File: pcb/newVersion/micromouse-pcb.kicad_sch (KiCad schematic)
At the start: 40 parts, among them J1_MotorEncoder1 Conn_01x06, J2_MotorEncoder1 Conn_01x06, J3 Conn_01x08, J4 Conn_01x08, Q1 BS170, Q2 TEFT4300, Q3 BS170, Q4 TEFT4300, Q5 BS170, Q6 TEFT4300, Q7 BS170, Q8 TEFT4300, SW1 SW_SPDT, U0 Teensy 4.1, U2 L7805

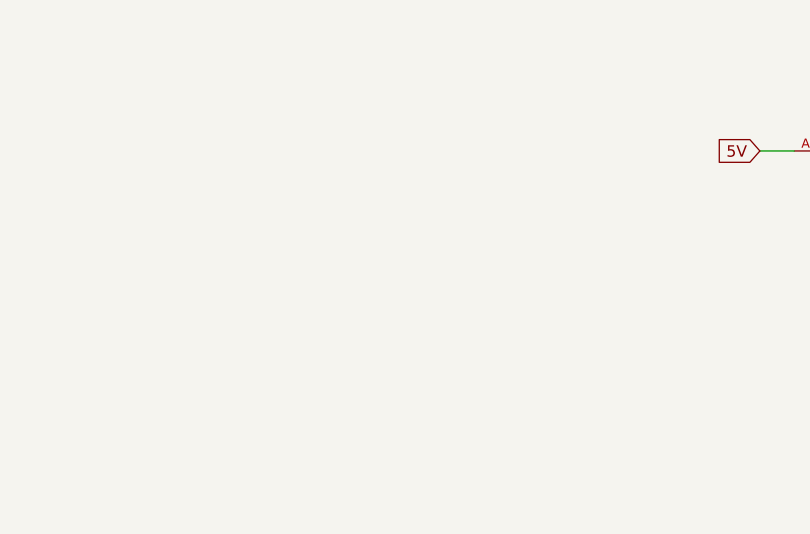
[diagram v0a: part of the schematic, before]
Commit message: changed board outline for ball caster mount
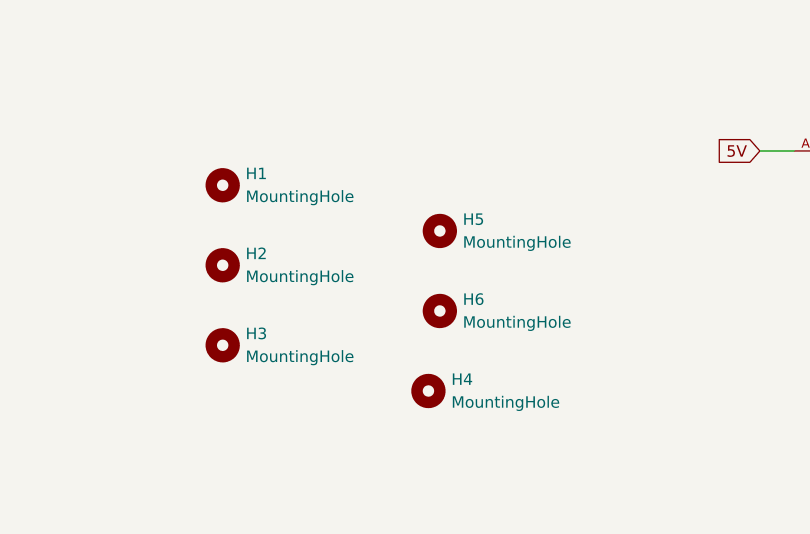
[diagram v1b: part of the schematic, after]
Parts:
- added H1, H2, H3, H4, H5, H6: MountingHole, MountingHole:MountingHole_4.3mm_M4, symbol Mechanical:MountingHole
- J1_MotorEncoder1, J2_MotorEncoder1: footprint Connector_PinHeader_2.54mm:PinHeader_1x06_P2.54mm_Vertical -> Connector_PinSocket_2.54mm:PinSocket_1x06_P2.54mm_Vertical
- J3, J4: footprint Connector_PinHeader_2.54mm:PinHeader_1x08_P2.54mm_Vertical -> Connector_PinSocket_2.54mm:PinSocket_1x08_P2.54mm_Vertical
